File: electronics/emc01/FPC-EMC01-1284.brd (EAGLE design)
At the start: 100 x 86.6 mm, 78 parts, among them J1 CONN-RECT-26PIN-2ROWSHROUDED, J10 ICSP, J11 CONN-RECT-16PIN-2ROW, J12 CONN-RECT-16PIN-2ROW, J13 CONN-RECT-16PIN-2ROW, J14 CONN-RECT-16PIN-2ROW, J15 CONN-RECT-16PIN-2ROW, J2 PCIE, J4 MOT-X, J5 MOT-Y, J6 MOT-Z, J7 CONN-RECT-3PINJST_PH_2MM, J8 CONN-RECT-3PINJST_PH_2MM, J9 CONN-RECT-3PINJST_PH_2MM, Q4 16Mhz, U10 MCP4728, U2 A4982, U3 A4982, U4 A4982, U5 ATMEGA1284P-AU

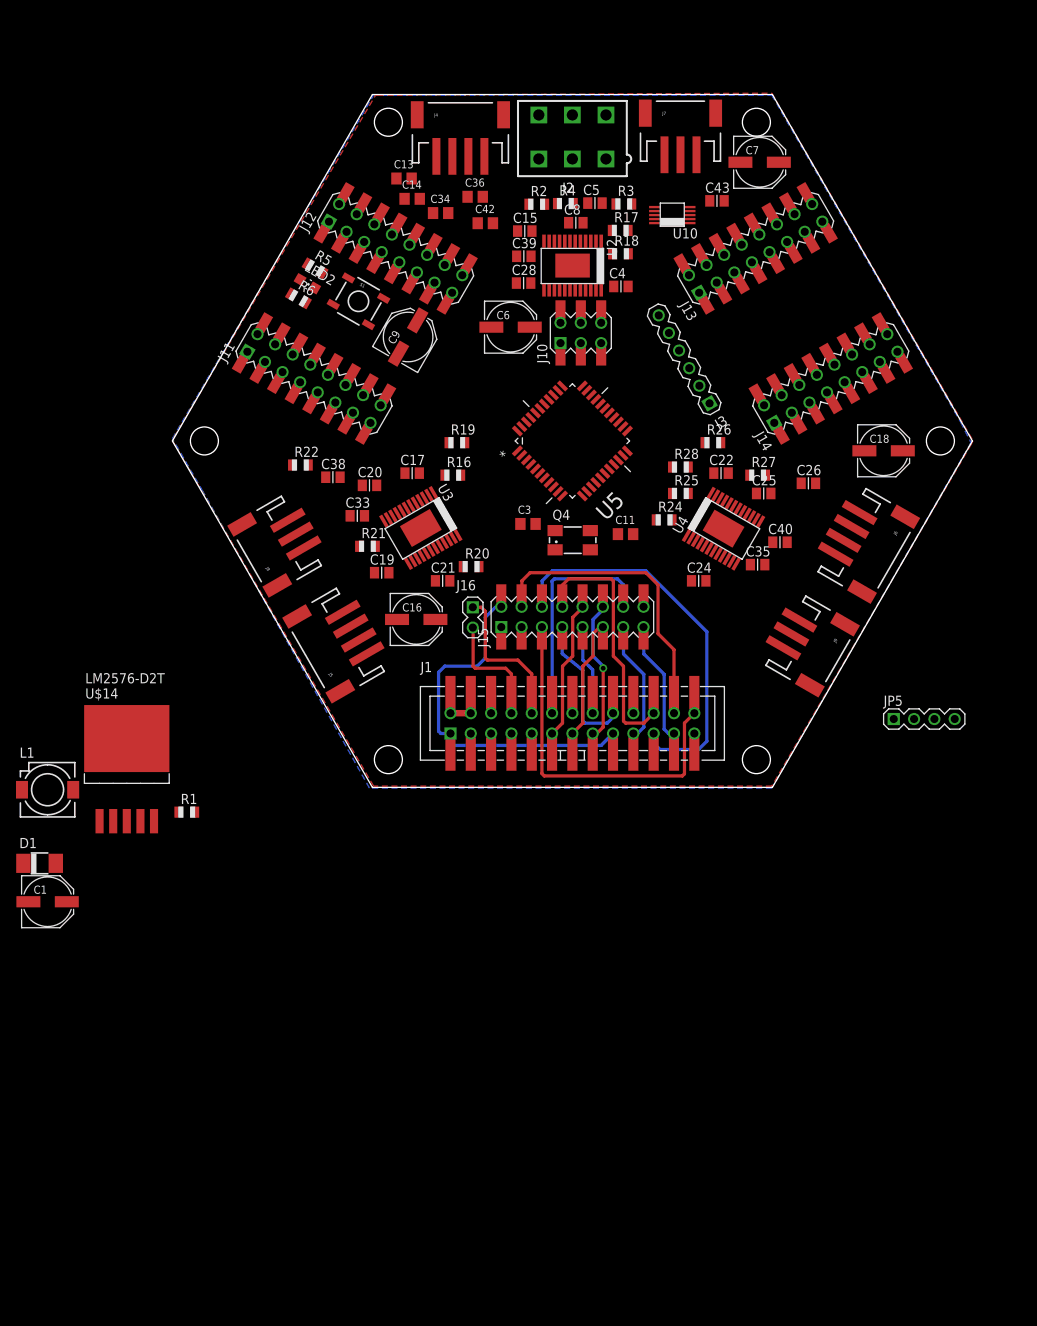
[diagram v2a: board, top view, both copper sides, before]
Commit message: Added StepStick to library, and updated EMC01 schematic/pcb
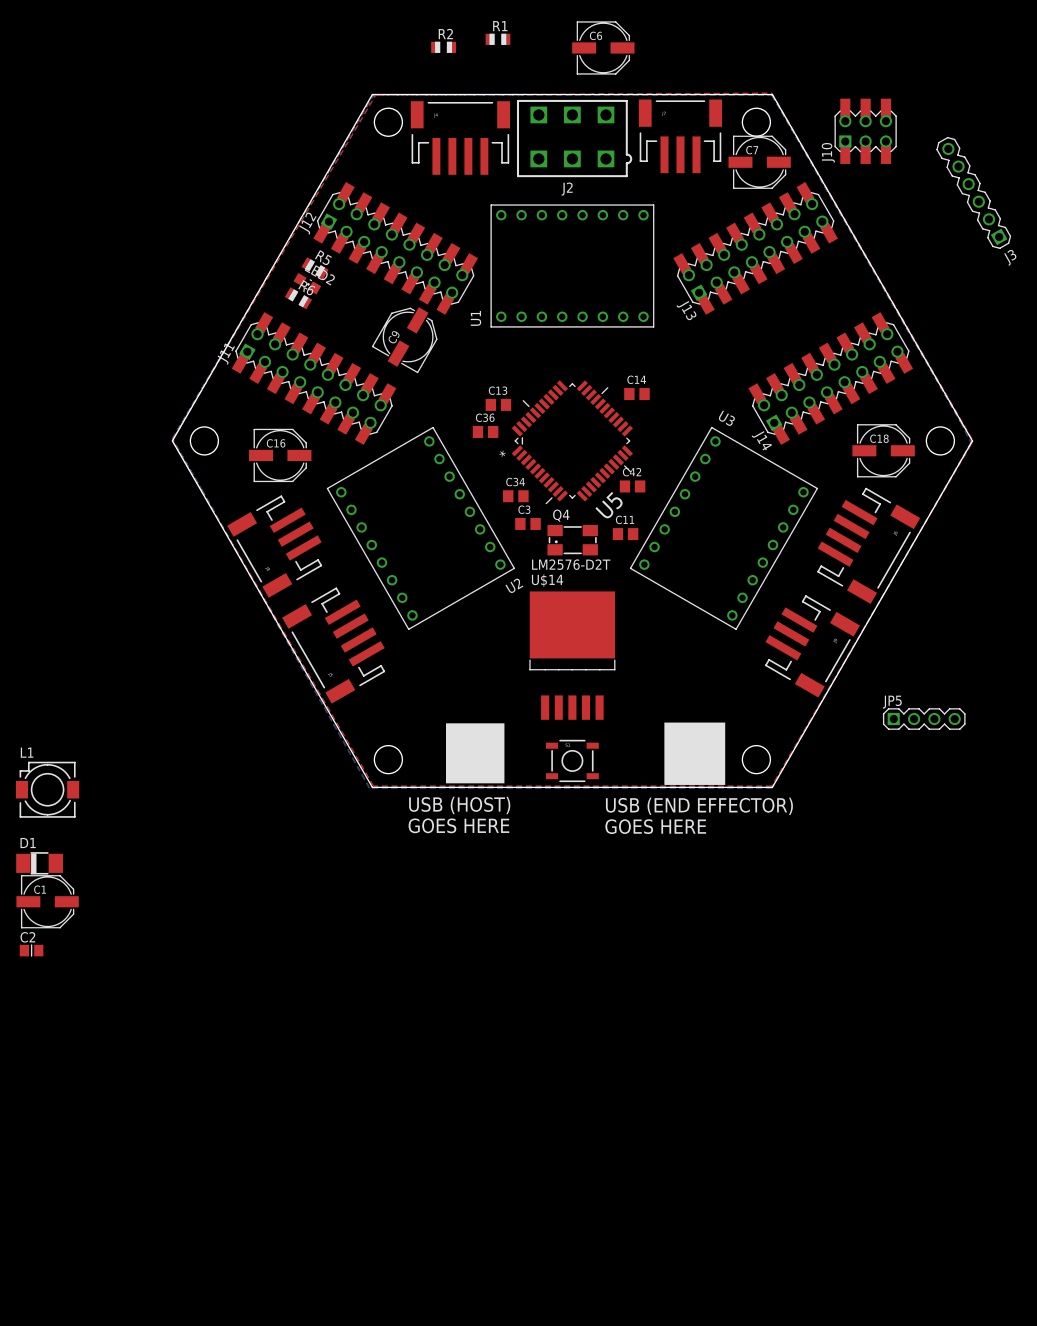
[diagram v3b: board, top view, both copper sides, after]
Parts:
- removed C15, C20, C25: 10uF, ipc-7351-capacitor:CAPC2012X145AN
- removed C17, C21, C22, C26, C28, C33, C35, C38, C39, C4, C40, C43, C5: 0.1uF, ipc-7351-capacitor:CAPC2012X145AN
- removed C19, C24, C8: 0.22uF, ipc-7351-capacitor:CAPC2012X145AN
- removed J1: CONN-RECT-26PIN-2ROWSHROUDED, FirePick:CONN-RECT-2.54MM-26-PIN-ROW-SHROUDED-SMTH
- removed J15: CONN-RECT-16PIN-2ROW, FirePick:CONN-RECT-2.54MM-16PIN-2ROW-SMTH
- removed J16: (no value), !con-lstb:MA02-1
- removed R16, R17, R18, R19, R24, R25: 0.11, adafruit:R0805
- removed R20, R26: 10k, adafruit:R0805
- removed R21, R22, R27, R28, R3, R4: 100k, adafruit:R0805
- removed U10: MCP4728, printrbot:MSOP10
- removed U4: A4982, printrbot:TSSOP-24
- added C2: 0.1, ipc-7351-capacitor:CAPC2012X145AN
- added U1: STEPSTICK, FirePick:STEPSTICK
- R2: value 10k -> 10K
- R5: value 100K -> 10K
- U2, U3: value A4982 -> STEPSTICK; device printrbot:TSSOP-24 -> FirePick:STEPSTICK
- moved R1 104.1 mm to (40.7, 100.2)
- moved S1 63.4 mm to (50.0, 10.0), turned to 0 degrees
- moved U$14 57.5 mm to (50.0, 27.0)
- moved J10 43.6 mm to (86.7, 88.7)
- moved J3 41.8 mm to (100.2, 81.0)
- moved U2 37.9 mm to (31.1, 39.1), turned to 210 degrees
- moved U3 37.9 mm to (68.9, 39.1), turned to 330 degrees
- moved C42 37.7 mm to (57.5, 44.3)
- moved C14 37.2 mm to (58.1, 55.9)
- moved C6 36.8 mm to (53.9, 99.1)
- moved C34 36.6 mm to (42.9, 43.1)
- moved C13 30.7 mm to (40.8, 54.5)
- moved C36 29.4 mm to (39.1, 51.1)
- moved C16 26.6 mm to (13.5, 48.2)
- moved R2 22.8 mm to (33.9, 99.2)
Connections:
- net N$3 renamed /POWER_SIG
- removed net +3V3_RASPI: J1.1, J1.17, J15.2
- removed net LCD_/E: J1.18, J15.7
- removed net LCD_DB4: J1.16, J15.9
- removed net LCD_DB5: J1.11, J15.10
- removed net LCD_DB6: J1.13, J15.11
- removed net LCD_DB7: J1.15, J15.12
- removed net LCD_RS: J1.22, J15.8
- removed net N$10: J4.4, U2.18
- removed net N$12: C5.1, U2.2
- removed net N$13: R2.1, U2.8
- removed net N$14: R17.1, U2.17
- removed net N$15: R18.1, U2.20
- removed net N$16: C4.2, U2.3
- removed net N$17: J4.2, U2.19
- removed net N$19: C8.2, U2.4
- removed net N$20: J4.3, U2.15
- removed net N$21: R4.2, U2.7, U2.9
- removed net N$23: J4.1, U2.22
- removed net N$29: C17.2, U3.1
- removed net N$30: C17.1, U3.2
- removed net N$32: R19.1, U3.20
- removed net N$34: R20.1, U3.8
- removed net N$35: C19.2, U3.4
- removed net N$36: R22.2, U3.7, U3.9
- removed net N$37: C21.2, U3.3
- removed net N$38: R16.1, U3.17
- removed net N$44: C22.2, U4.1
- removed net N$45: C22.1, U4.2
- removed net N$46: R24.1, U4.17
- removed net N$47: R25.1, U4.20
- removed net N$49: R26.1, U4.8
- removed net N$50: C24.2, U4.4
- removed net N$51: R28.2, U4.7, U4.9
- removed net N$52: C26.2, U4.3
- removed net PANEL_ENC_A: J1.26, J15.5
- removed net PANEL_ENC_B: J1.21, J15.6
- removed net PANEL_ENC_SW: J1.24, J15.4
- removed net PANEL_LED_GRN: J1.19, J15.13
- removed net PANEL_LED_RED: J1.12, J15.14
- removed net PANEL_PUSHBTN: J1.23, J15.15
- removed net RASPI_RXD: J1.10, J16.1
- removed net RASPI_TXD: J1.8, J16.2
- removed net VREF_X: C39.1, U10.9, U2.12
- removed net VREF_Y: C38.1, U10.8, U3.12
- removed net VREF_Z: C40.1, U10.7, U4.12
- new net N$6: J4.4, U1.2B
- new net N$7: J4.3, U1.2A
- new net N$8: J4.2, U1.1A
- new net N$9: J4.1, U1.1B
- net !XYZ-ENABLE: now also R2.1, U1.!ENABLE!; no longer R21.2, R27.2, R3.2, U2.23, U3.23, U4.23
- net !~RESET: now also C2.1
- net +5V: now also R2.2, U1.MS1, U1.MS2, U1.MS3, U1.VDD; no longer C15.2, C20.2, C25.2, C43.2, J1.2, J1.4, J15.1, R21.1, R22.1, R27.1, R28.1, R3.1, R4.1, U10.1, U10.4, U2.10, U2.5, U2.6, U3.10, U3.5, U3.6, U4.10, U4.5, U4.6
- net 12V: now also U1.VMOT; no longer C21.1, C26.1, C28.1, C33.1, C35.1, C4.1, U2.16, U2.21, U3.16, U3.21, U4.16, U4.21
- net DTR: now also C2.2
- net GND: now also U1.GND, U1.GND@2; no longer C15.1, C19.1, C20.1, C24.1, C25.1, C28.2, C33.2, C35.2, C38.2, C39.2, C40.2, C43.1, C8.1, J1.14, J1.20, J1.25, J1.6, J1.9, J15.16, J15.3, R16.2, R17.2, R18.2, R19.2, R2.2, R20.2, R24.2, R25.2, R26.2, U10.10, U2.13, U2.24, U2.PAD, U3.13, U3.24, U3.PAD, U4.13, U4.24, U4.PAD
- net N$11: now also U1.!RESET!, U1.!SLEEP!; no longer C5.2, U2.1
- net N$24: no longer U3.19
- net N$25: no longer U3.18
- net N$26: no longer U3.15
- net N$31: no longer U3.22
- net N$39: no longer U4.18
- net N$40: no longer U4.19
- net N$41: no longer U4.15
- net N$53: no longer U4.22
- net SCL: no longer U10.2
- net SDA: no longer U10.3
- net X_DIR: now also U1.STEP; no longer U2.14
- net X_STEP: now also U1.DIR; no longer U2.11
- net Y_DIR: no longer U3.14
- net Y_STEP: no longer U3.11
- net Z_DIR: no longer U4.14
- net Z_STEP: no longer U4.11
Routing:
- net PANEL_ENC_B: track 49.8 -> 0.00 mm
- net +3V3_RASPI: track 45.3 -> 0.00 mm
- net PANEL_ENC_A: track 44.5 -> 0.00 mm
- net PANEL_ENC_SW: track 38.2 -> 0.00 mm
- net LCD_RS: track 32.0 -> 0.00 mm
- net PANEL_LED_RED: track 28.6 -> 0.00 mm
- net RASPI_RXD: track 19.1 -> 0.00 mm
- net LCD_DB7: track 17.7 -> 0.00 mm, vias 1 -> 0
- net LCD_/E: track 17.7 -> 0.00 mm
- net LCD_DB5: track 17.4 -> 0.00 mm
- net PANEL_PUSHBTN: track 15.3 -> 0.00 mm
- net PANEL_LED_GRN: track 15.2 -> 0.00 mm
- net LCD_DB6: track 15.1 -> 0.00 mm
- net RASPI_TXD: track 14.9 -> 0.00 mm
- net LCD_DB4: track 11.3 -> 0.00 mm
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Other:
- board text added: "USB (END EFFECTOR) GOES HERE"
- board text added: "USB (HOST) GOES HERE"

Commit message: fixing I2C connectors, adding FTDI, adding sch for motor controllers
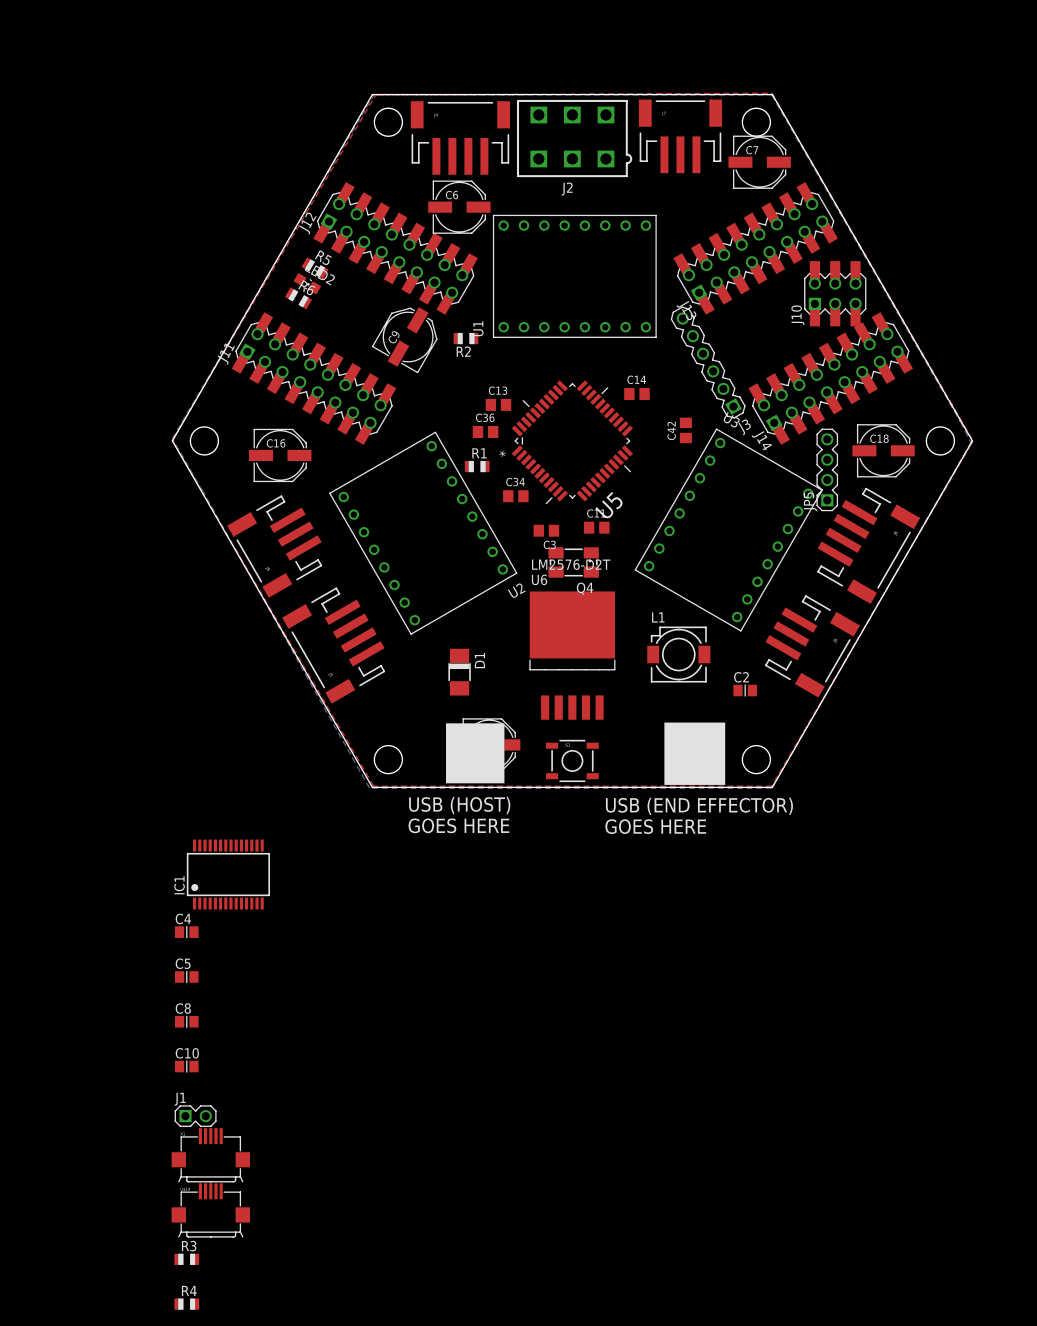
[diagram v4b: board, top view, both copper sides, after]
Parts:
- added C10, C5, C8: 0.1uF, ipc-7351-capacitor:CAPC2012X145AN
- added C4: 0.33uF, ipc-7351-capacitor:CAPC2012X145AN
- added IC1: FT232RL, ftdichip:SSOP28
- added J1: (no value), !con-lstb:MA02-1
- added R3, R4: 10K, adafruit:R0805
- added U6: LM2576-D2T, FirePick:D2PAK
- added X1: USB-MICROB, SparkFun:USB-MICROB
- R1: value 10k -> 10K
- U$14: value LM2576-D2T -> USB-MICROB-I2CUSB-; device FirePick:D2PAK -> SparkFun:USB-MICROB-I2C
- moved C2 94.9 mm to (71.6, 18.8)
- moved U$14 86.6 mm to (4.80, -46.9)
- moved L1 80.7 mm to (63.3, 23.3)
- moved C1 58.6 mm to (39.6, 12.0)
- moved D1 57.7 mm to (35.9, 21.1), turned to 270 degrees
- moved R1 53.5 mm to (38.1, 46.8)
- moved J3 39.4 mm to (67.0, 59.8)
- moved R2 36.5 mm to (36.7, 62.8), turned to 180 degrees
- moved JP5 33.4 mm to (81.9, 46.4), turned to 90 degrees
- moved C6 26.8 mm to (35.9, 79.2)
- moved J10 20.7 mm to (82.9, 68.4)
- moved C42 9.67 mm to (64.2, 51.3), turned to 90 degrees
- moved C11 3.69 mm to (53.0, 39.2)
- moved Q4 2.79 mm to (50.2, 34.8), turned to 180 degrees
- moved C3 2.45 mm to (46.8, 38.8), turned to 180 degrees
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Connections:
- removed net !~RESET: C2.1, J10.2, R5.1, S1.3, S1.4, U5.4
- removed net /POWER_SIG: R1.1, U5.44
- removed net N$25: J5.4
- removed net N$26: J5.3
- removed net N$31: J5.1
- removed net N$39: J6.4
- removed net N$40: J6.2
- removed net N$41: J6.3
- removed net N$53: J6.1
- new net !RESET: C2.1, J1.1, J10.2, R5.1, S1.3, S1.4, U5.4
- new net N$10: C8.2, J1.2
- new net N$12: C10.1, IC1.17
- new net N$13: J5.3, U2.2A
- new net N$14: J5.2, U2.1A
- new net N$15: J5.1, U2.1B
- new net N$16: U2.!RESET!, U2.!SLEEP!
- new net N$17: J6.4, U3.2B
- new net N$18: J6.3, U3.2A
- new net N$19: J6.2, U3.1A
- new net N$20: J6.1, U3.1B
- new net N$3: C8.1, IC1.2
- new net USB_D+: IC1.15, X1.D+
- new net USB_D-: IC1.16, X1.D-
- new net Z-PROBE: R1.2, U5.44
- net !XYZ-ENABLE: now also R3.1, R4.1, U2.!ENABLE!, U3.!ENABLE!
- net +5V: now also C4.1, C5.1, IC1.20, IC1.4, R1.1, R3.2, R4.2, U$14.+5V, U2.MS1, U2.MS2, U2.MS3, U2.VDD, U3.MS1, U3.MS2, U3.MS3; no longer J12.7, J13.8, J14.7, J14.8
- net 12V: now also J11.3, J11.4, J12.3, J12.4, J13.3, J13.4, J14.3, J14.4, U2.VMOT, U3.VMOT, U6.1; no longer U$14.1
- net AVR_RXD: now also IC1.1
- net AVR_TXD: now also IC1.5
- net GND: now also C10.2, C4.2, C5.2, IC1.18, IC1.21, IC1.25, IC1.26, IC1.7, J12.7, J13.8, J14.7, J14.8, J2.6, U$14.GND, U2.GND, U2.GND@2, U3.GND, U3.GND@2, U6.3, U6.5, U6.6, X1.GND; no longer J11.3, J11.4, J12.3, J12.4, J13.3, J13.4, J14.3, J14.4, U$14.3, U$14.5, U$14.6
- net N$1: now also J5.4, U2.2B; no longer J2.6, R1.2
- net N$24: now also U3.!RESET!, U3.!SLEEP!; no longer J5.2
- net N$4: now also U6.2; no longer U$14.2
- net N$5: now also U6.4; no longer U$14.4
- net SCL: now also U$14.SCL
- net SDA: now also U$14.SDA
- net Y_DIR: now also U2.STEP
- net Y_STEP: now also U2.DIR
- net Z_DIR: now also U3.STEP
- net Z_STEP: now also U3.DIR

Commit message: board partially routed
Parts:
- C11, C3: value 22pf -> 22pF
- C2: value 0.1 -> 0.1uF
- moved R4 116.5 mm to (60.1, 43.0), turned to 270 degrees
- moved R3 90.5 mm to (42.1, 28.8), turned to 270 degrees
- moved U$14 81.8 mm to (63.9, 9.60)
- moved C10 63.4 mm to (43.9, 19.1), turned to 90 degrees
- moved X1 59.4 mm to (37.4, 9.60)
- moved J1 56.9 mm to (27.1, 17.1), turned to 90 degrees
- moved C8 52.0 mm to (28.4, 22.1), turned to 270 degrees
- moved C2 48.8 mm to (22.9, 15.3)
- moved C5 45.1 mm to (30.8, 17.6)
- moved C4 44.3 mm to (31.1, 21.8), turned to 270 degrees
- moved IC1 39.0 mm to (37.3, 20.4), turned to 270 degrees
- moved C1 32.9 mm to (72.2, 16.4), turned to 180 degrees
- moved D1 29.6 mm to (65.5, 19.4), turned to 90 degrees
- moved JP5 11.2 mm to (92.4, 50.3)
- moved R1 10.1 mm to (38.3, 56.9)
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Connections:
- net !RESET: no longer J1.1
- net DTR: now also J1.1
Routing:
- net N$5: track 0.00 -> 27.5 mm
- net N$4: track 0.00 -> 21.1 mm
- net !XYZ-ENABLE: track 0.00 -> 20.9 mm
- net 12V: track 0.00 -> 18.4 mm
- net GND: track 0.00 -> 17.7 mm
- net N$14: track 0.00 -> 12.9 mm, vias 0 -> 1
- net XTAL2: track 0.00 -> 12.6 mm
- net N$13: track 0.00 -> 12.6 mm
- net N$18: track 0.00 -> 12.5 mm, vias 0 -> 1
- net XTAL1: track 0.00 -> 12.4 mm
- net N$20: track 0.00 -> 11.8 mm, vias 0 -> 1
- net N$19: track 0.00 -> 11.8 mm
- net N$1: track 0.00 -> 11.4 mm, vias 0 -> 1
- net N$15: track 0.00 -> 11.1 mm
- net N$17: track 0.00 -> 10.9 mm
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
